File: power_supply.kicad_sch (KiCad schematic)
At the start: 38 parts, among them U11 TPS62151, U2 2.2uH, U3 2.2uH, U5 TPS62151

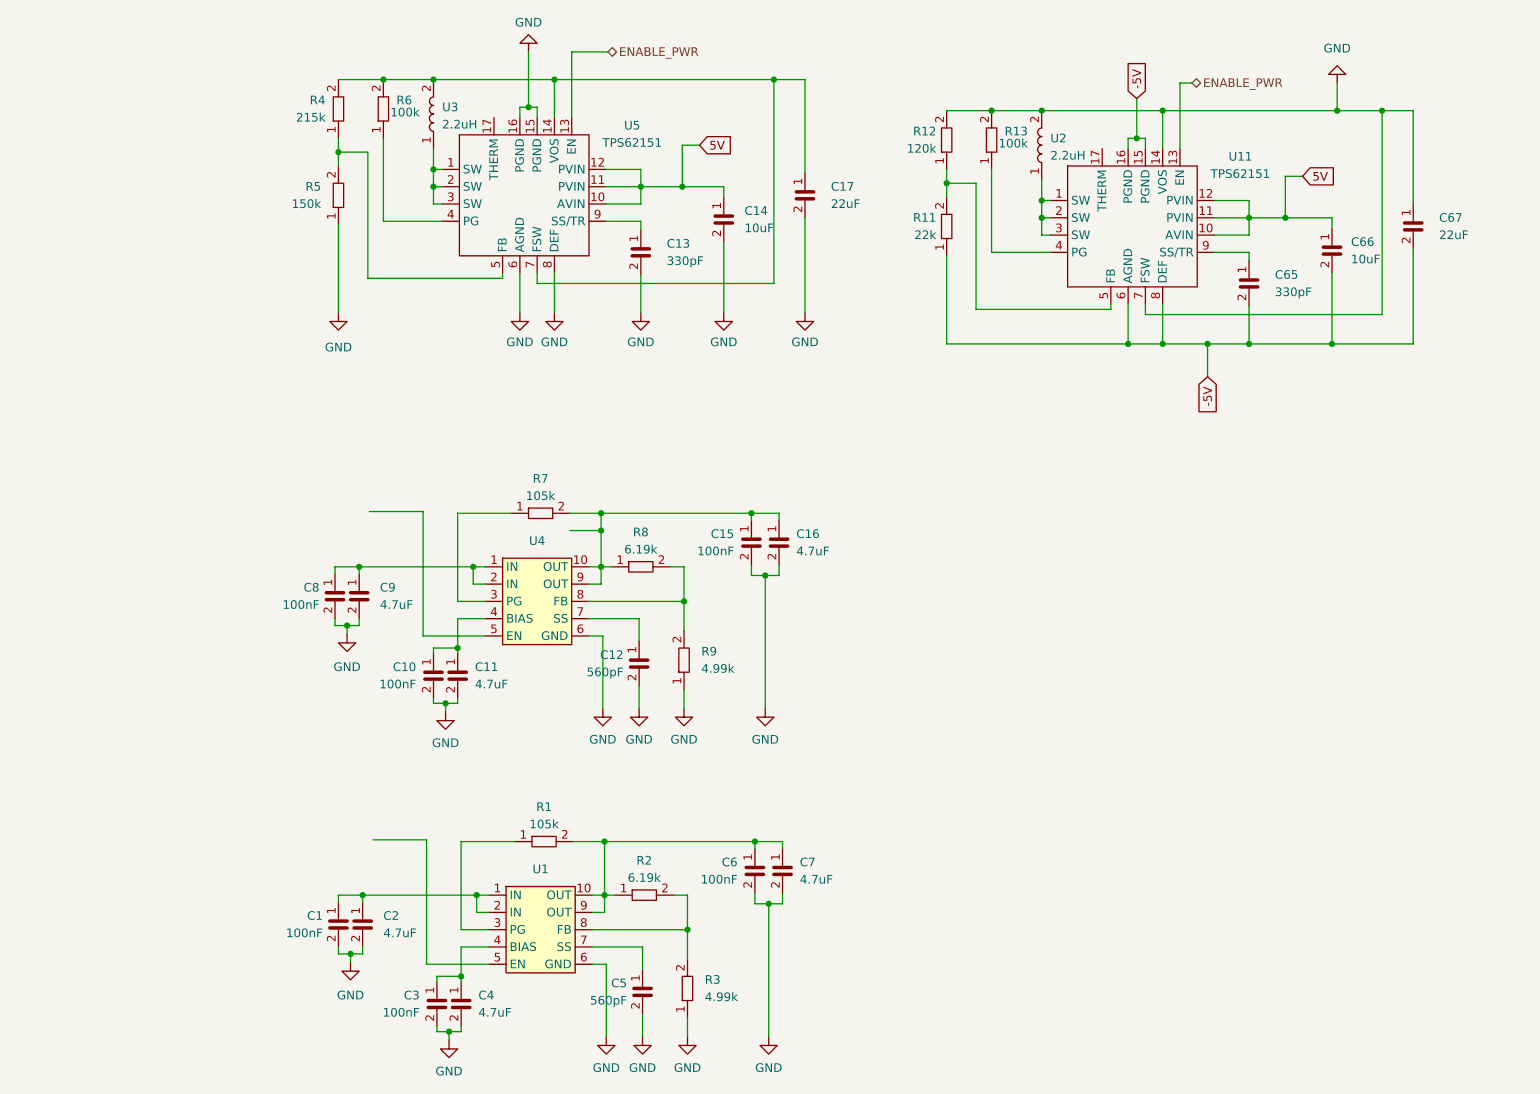
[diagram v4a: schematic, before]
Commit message: Changed global to hierarchichal lables, reorganized main sheet to get pins to connector.
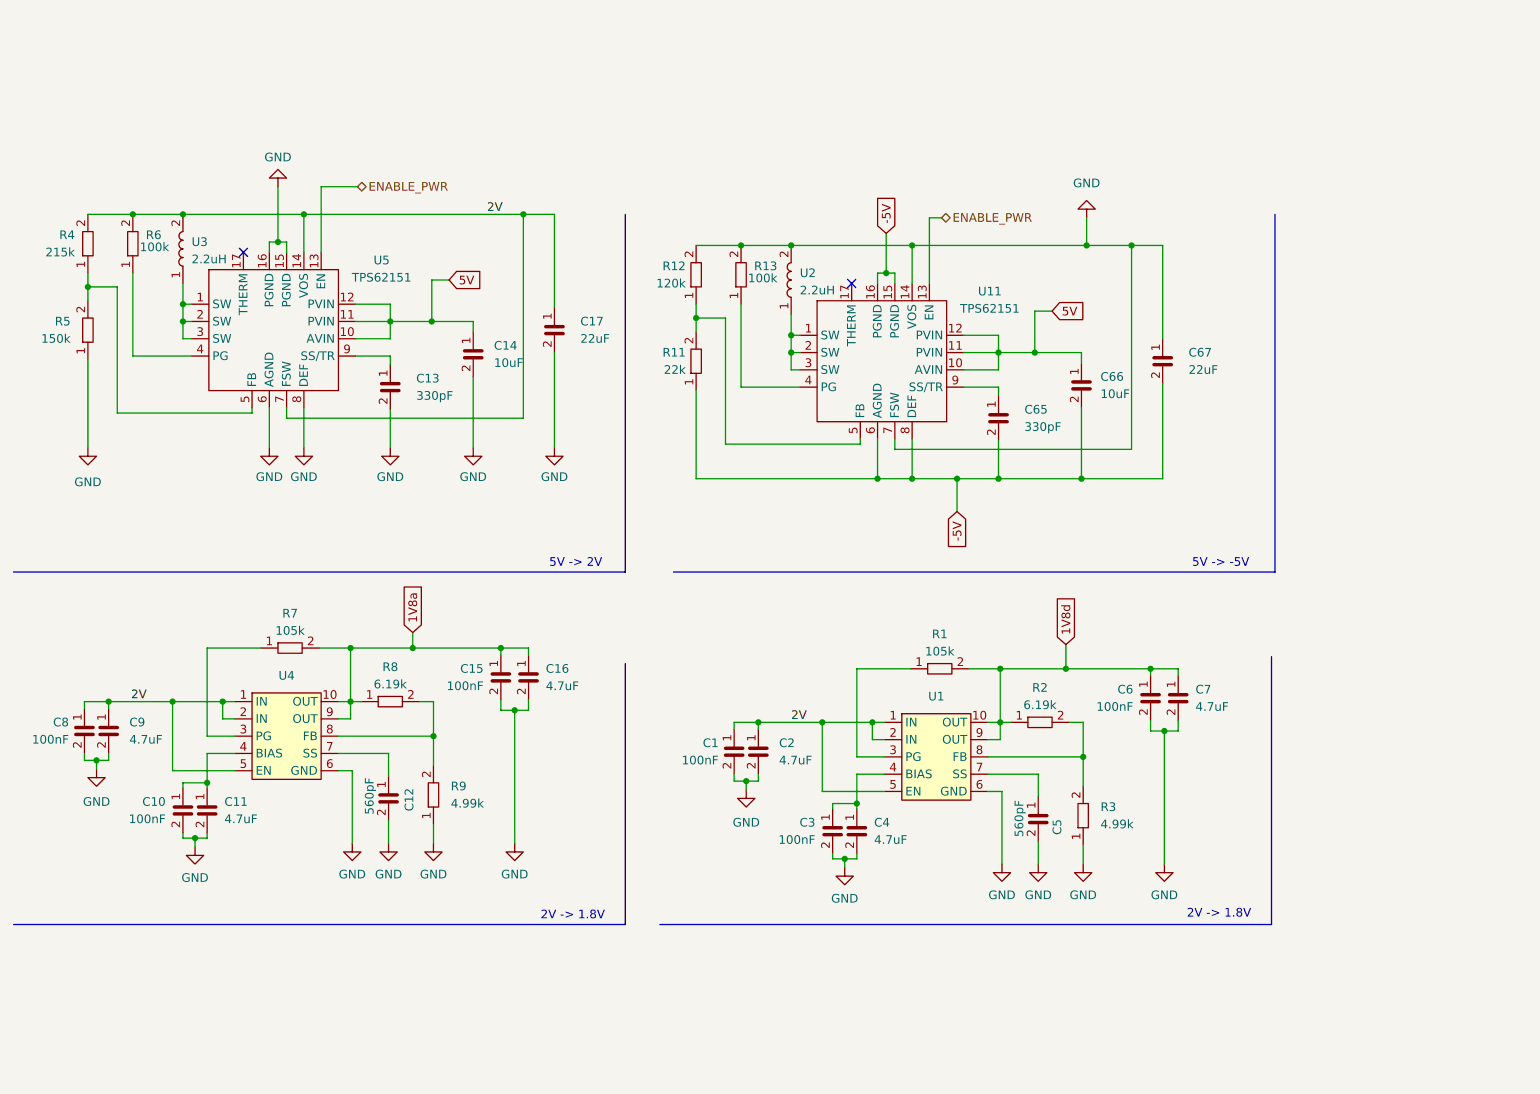
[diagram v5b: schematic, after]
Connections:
- net 1V8a: now reaches C15.1, C16.1, R7.2, R8.1, U4.10 (OUT), U4.9 (OUT)
- net 2V: now reaches C8.1, C9.1, U4.1 (IN), U4.2 (IN)
- net 2V: now also C1.1, C17.1, C2.1, R4.2, R6.2, U1.1 (IN), U1.2 (IN), U1.5 (EN), U3.2, U4.5 (EN), U5.14 (VOS), U5.7 (FSW)
- net 1V8d: now reaches C6.1, C7.1, R1.2, R2.1, U1.10 (OUT), U1.9 (OUT)
- no-connect marks 0 -> 2
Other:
- note added: "2V -> 1.8V"
- note added: "5V -> -5V"
- note added: "5V -> 2V"
- moved on the sheet: C1, C10, C11, C12, C13, C14, C15, C16, C17, C2, C3, C4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

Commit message: Added connector to all sheets.
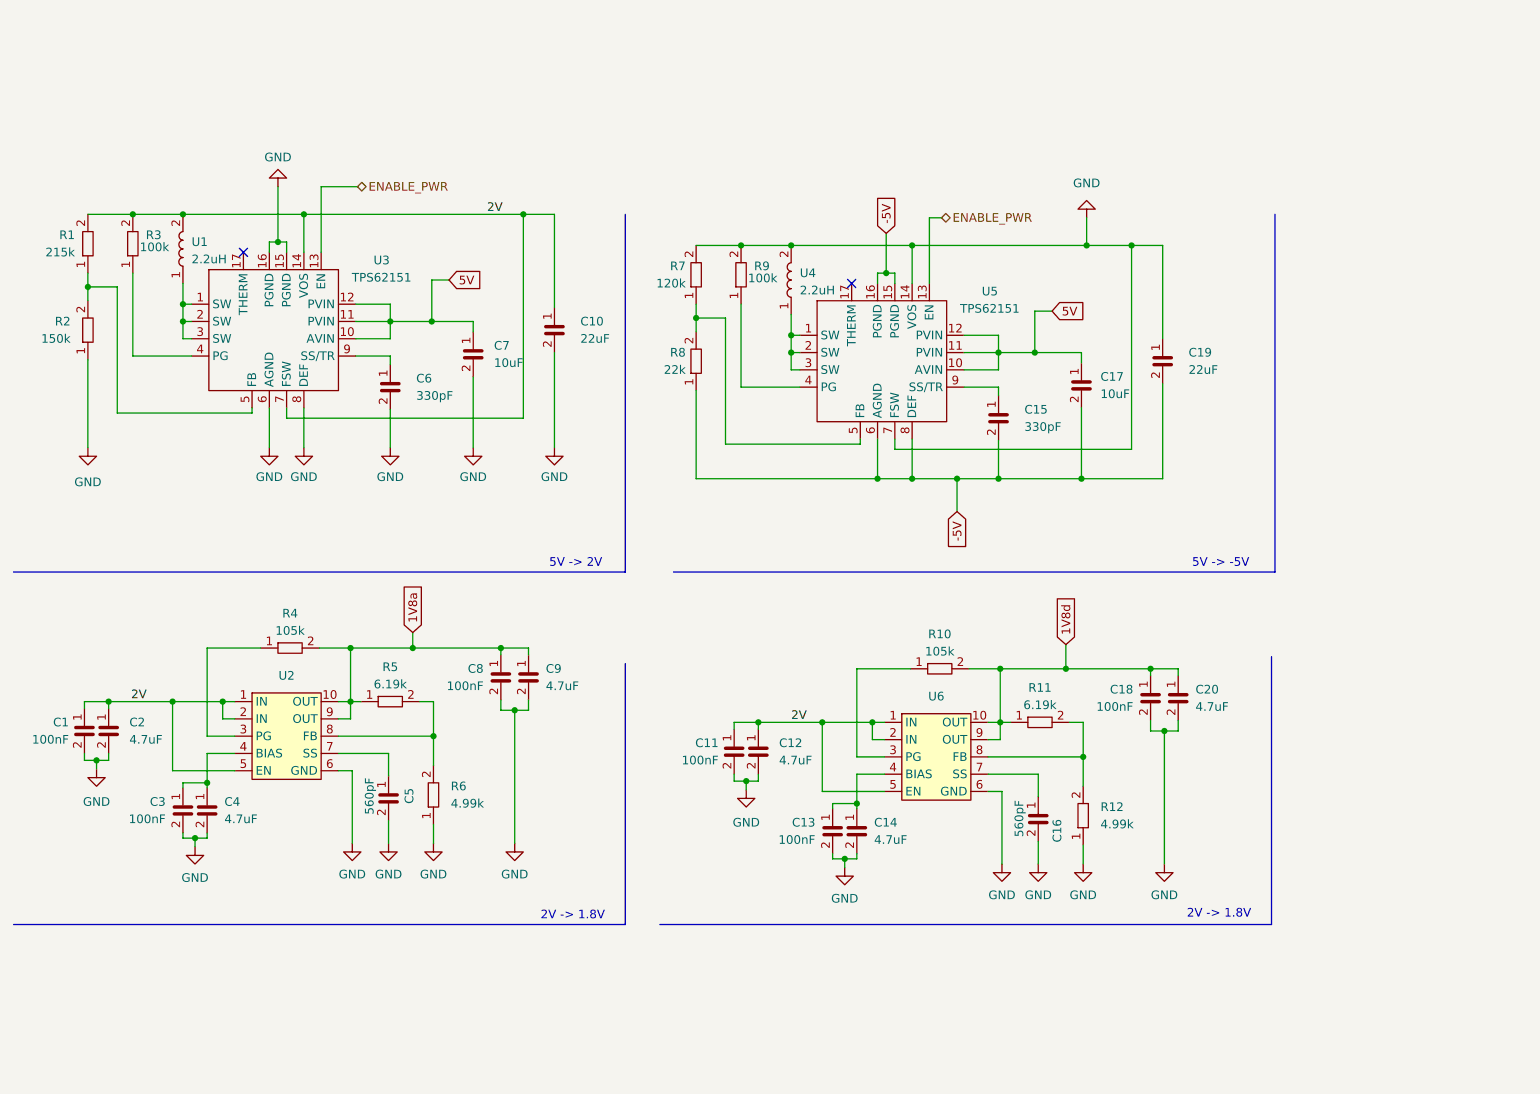
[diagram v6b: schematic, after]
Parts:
- renumbered C8 to C1, C17 to C10, C1 to C11, C2 to C12, C3 to C13, C4 to C14, C65 to C15, C5 to C16, C66 to C17, C6 to C18, C67 to C19, C9 to C2, C7 to C20, C10 to C3, C11 to C4, C12 to C5, C13 to C6, C14 to C7, C15 to C8, C16 to C9, R4 to R1, R1 to R10, R2 to R11, R3 to R12, R5 to R2, R6 to R3, R7 to R4, R8 to R5, R9 to R6, R12 to R7, R11 to R8, R13 to R9, U3 to U1, U4 to U2, U5 to U3, U2 to U4, U11 to U5, U1 to U6

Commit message: Schematic finished, ready for review.
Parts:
- U1: renamed from U2; value ~ -> TPS74801
- U4: renamed from U6; value ~ -> TPS74801
- renumbered U1 to L1, U4 to L2, U3 to U2, U5 to U3

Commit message: Layout erster Entwurf fertig.
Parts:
- removed C11, C13, C18: C0402_100nF_50V, Capacitor_SMD:C_0402_1005Metric, symbol Jojos_Lib:C0402_100nF_50V
- removed C12, C14, C20: C0402_4.7uF_6.3V, Capacitor_SMD:C_0402_1005Metric, symbol Jojos_Lib:C0402_4.7uF_6.3V
- removed C16: C0402_560p_10V, Capacitor_SMD:C_0402_1005Metric, symbol Jojos_Lib:C0402_560pF_10V
- removed R10: R0402_105k, Resistor_SMD:R_0402_1005Metric, symbol Jojos_Lib:R0402_105k
- removed R11: R0402_6.19k, Resistor_SMD:R_0402_1005Metric, symbol Jojos_Lib:R0402_6.19k
- removed R12: R0402_4.99k, Resistor_SMD:R_0402_1005Metric, symbol Jojos_Lib:R0402_4.99k
- removed U4: TPS74801, Package_SON:VSON-10-1EP_3x3mm_P0.5mm_EP1.65x2.4mm, symbol Jojos_Lib:TPS74801DRCR
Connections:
- net GND: now also U1.11 (THERM), U2.17 (THERM), U3.17 (THERM)
- no-connect marks 2 -> 0
